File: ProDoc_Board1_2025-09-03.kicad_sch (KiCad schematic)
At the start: 14 parts, among them CN10 A2502-WV02, CN11 A2502-WV02, CN2 B04B-XNISK-A-1(LF)(SN), CN3 B04B-XNISK-A-1(LF)(SN), CN4 B04B-XNISK-A-1(LF)(SN), CN7 XH2.54-5PIN, CN8 A2502-WV02, CN9 A2502-WV02, J1 Conn_01x05_Pin, U3 Ra-02, U4 XL 4005

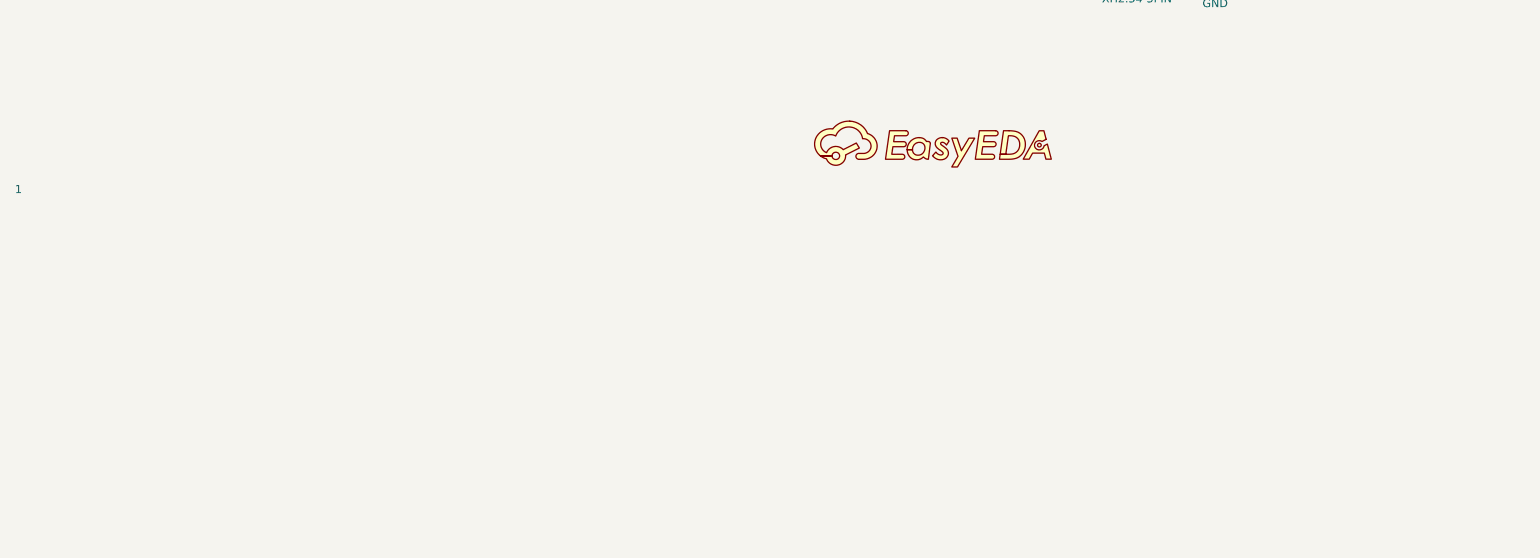
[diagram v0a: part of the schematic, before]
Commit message: added IC
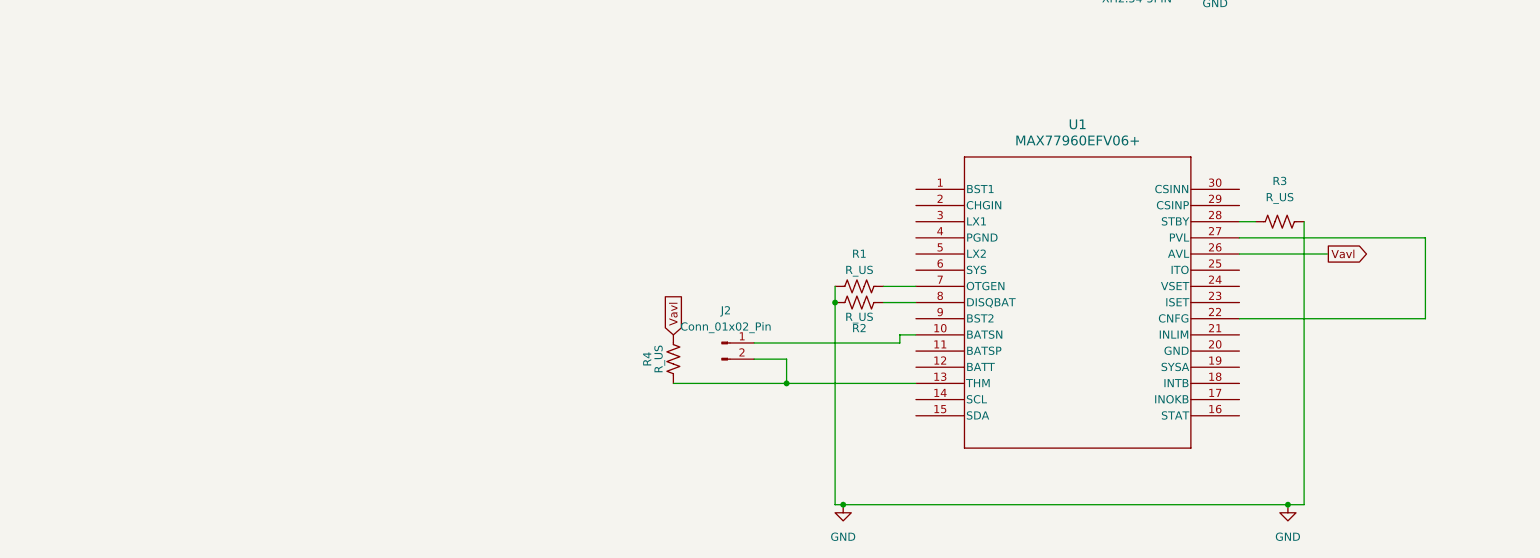
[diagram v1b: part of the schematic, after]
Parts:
- removed 1: ~, symbol ProDoc_Boa-easyedapro:Drawing-Symbol_A4
- added J2: Conn_01x02_Pin, symbol Connector:Conn_01x02_Pin
- added R1, R2, R3, R4: R_US, symbol Device:R_US
- added U1: MAX77960EFV06+, ProDoc_Board1_2025-09-03:MAXIM, symbol MAXIM:MAX77960EFV06+
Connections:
- net GND: now also R1.1, R2.1, R3.2
- new net: R1.2, U1.7 (OTGEN)
- new net: J2.1 (Pin_1), U1.10 (BATSN)
- new net: J2.2 (Pin_2), R4.2, U1.13 (THM)
- new net: U1.22 (CNFG), U1.27 (PVL)
- new net: R3.1, U1.28 (STBY)
- new net: R2.2, U1.8 (DISQBAT)
- new net Vavl: R4.1, U1.26 (AVL)

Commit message: schenatic done
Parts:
- removed U1: MAX77960EFV06+, ProDoc_Board1_2025-09-03:MAXIM, symbol MAXIM:MAX77960EFV06+
- added C1: C_STAT, Capacitor_SMD:C_1210_3225Metric, symbol Device:C_Small
- added C10: C_CSINN, Capacitor_SMD:C_1210_3225Metric, symbol Device:C_Small
- added C11: C_CINP, Capacitor_SMD:C_1210_3225Metric, symbol Device:C_Small
- added C12: C_DIFF, Capacitor_SMD:C_1210_3225Metric, symbol Device:C_Small
- added C2: C_PVL, Capacitor_SMD:C_0402_1005Metric, symbol Device:C_Small
- added C3: C_AVL, Capacitor_SMD:C_0402_1005Metric, symbol Device:C_Small
- added C4: C_BST2, Capacitor_SMD:C_0402_1005Metric, symbol Device:C_Small
- added C5: C_BST1, Capacitor_SMD:C_0402_1005Metric, symbol Device:C_Small
- added C6: C_BATT, Capacitor_SMD:C_0805_2012Metric, symbol Device:C_Small
- added C7: C_OUT1, Capacitor_SMD:C_1210_3225Metric_Pad1.33x2.70mm_HandSolder, symbol Device:C_Small
- added C8: C_OUT2, Capacitor_SMD:C_1210_3225Metric_Pad1.33x2.70mm_HandSolder, symbol Device:C_Small
- added C9: C_CHGIN, Capacitor_SMD:C_1210_3225Metric, symbol Device:C_Small
- added D1: LED, Diode_SMD:D_01005_0402Metric, symbol Device:LED
- added D3: D_Schottky_Small, Diode_SMD:D_SOD-323, symbol Device:D_Schottky_Small
- added L1: L, ProDoc_Board1_2025-09-03:CMLE063T-2R2MS, symbol Device:L
- added R10: R_ITO, Resistor_SMD:R_0805_2012Metric, symbol Device:R_US
- added R11: R_VSET, Resistor_SMD:R_0805_2012Metric, symbol Device:R_US
- added R12: R_INTB, Resistor_SMD:R_0805_2012Metric, symbol Device:R_US
- added R13: R_SDA, Resistor_SMD:R_0805_2012Metric, symbol Device:R_US
- added R14: R_SCL, Resistor_SMD:R_0805_2012Metric, symbol Device:R_US
- added R15, R16: R_SENSE, Resistor_SMD:R_1206_3216Metric, symbol Device:R_US
- added R17: R_CINN, Resistor_SMD:R_1206_3216Metric, symbol Device:R_US
- added R5: R_ISET, Resistor_SMD:R_0805_2012Metric, symbol Device:R_US
- added R6: R_INOKB, Resistor_SMD:R_0805_2012Metric, symbol Device:R_US
- added R7: R_STAT, Resistor_SMD:R_0805_2012Metric, symbol Device:R_US
- added R8: R_PVL, Resistor_SMD:R_0805_2012Metric, symbol Device:R_US
- added R9: R_INLIM, Resistor_SMD:R_0805_2012Metric, symbol Device:R_US
- added U1: MAX77961EFV06+, ProDoc_Board1_2025-09-03:MAX77961, symbol MAX77961:MAX77961EFV06+
- CN10: value A2502-WV02 -> BATT
- CN11: value A2502-WV02 -> CHGIN
- J2: footprint (none) -> Connector_JST:JST_SH_BM02B-SRSS-TB_1x02-1MP_P1.00mm_Vertical
- R1: value R_US -> R_OTGEN; footprint (none) -> Resistor_SMD:R_0805_2012Metric
- R2: value R_US -> R_DISQBAT; footprint (none) -> Resistor_SMD:R_0805_2012Metric
- R3: value R_US -> R_STBY; footprint (none) -> Resistor_SMD:R_0805_2012Metric
- R4: value R_US -> R_TB; footprint (none) -> Resistor_SMD:R_0805_2012Metric
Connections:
- net GND: now also CN11.1, J2.1 (Pin_1), C1.2, C10.2, C11.1, C2.2, C3.2, C6.2, C7.2, C8.2, C9.2, R10.2, R11.2, R5.2, R9.2, U1.10 (BATSN), U1.20 (GND), U1.4 (PGND)
- net BATT+: now reaches CN10.2
- net BATT+: now also C6.1, U1.11 (BATSP), U1.12 (BATT); no longer CN11.1
- net at R1.2: now also U1.7 (OTGEN)
- net at J2.2 (Pin_2), R4.2: now also U1.13 (THM)
- net at R3.1: now also U1.28 (STBY)
- net at R2.2: now also U1.8 (DISQBAT)
- net STAT: now reaches H1.36
- net STAT: now also C1.1, D3.2 (A), R7.1
- net at CN11.2: now also R15.1, R16.2; no longer D2.2 (A)
- net Vavl renamed PULLUP
- net PULLUP: now also C3.1, D1.2 (A), R12.2, R13.1, R14.1, R7.2, R8.2, U1.26 (AVL)
- new net: R14.2, U1.14 (SCL)
- new net: D3.1 (K), U1.16 (STAT)
- new net: R11.1, U1.24 (VSET)
- new net: C2.1, R8.1, U1.22 (CNFG), U1.27 (PVL)
- new net: R6.1, U1.17 (INOKB)
- new net: D1.1 (K), R6.2
- new net: C5.1, U1.1 (BST1)
- new net: C5.2, L1.1, U1.3 (LX1)
- new net: R10.1, U1.25 (ITO)
- new net: R9.1, U1.21 (INLIM)
- new net: R13.2, U1.15 (SDA)
- new net: C4.1, L1.2, U1.5 (LX2)
- new net: C4.2, U1.9 (BST2)
- new net: R12.1, U1.18 (INTB)
- new net: R5.1, U1.23 (ISET)
- new net CHGIN: C9.1, R15.2, R17.2, U1.2 (CHGIN)
- new net CSINN: C10.1, C12.2, R17.1, U1.30 (CSINN)
- new net CSINP: C11.2, C12.1, R16.1, U1.29 (CSINP)
- new net SYS: C7.1, C8.1, D2.2 (A), U1.19 (SYSA), U1.6 (SYS)
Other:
- moved on the sheet: CN10, CN11, D2, R4

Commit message: layout started
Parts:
- C10, C11, C12: footprint Capacitor_SMD:C_1210_3225Metric -> Capacitor_SMD:C_0402_1005Metric
- C7, C8: footprint Capacitor_SMD:C_1210_3225Metric_Pad1.33x2.70mm_HandSolder -> Capacitor_SMD:C_1210_3225Metric
- CN10, CN11: footprint Connector_JST:JST_SH_BM02B-SRSS-TB_1x02-1MP_P1.00mm_Vertical -> Connector_JST:JST_VH_B2P-VH_1x02_P3.96mm_Vertical
- R16: value R_SENSE -> R_CSINP; footprint Resistor_SMD:R_1206_3216Metric -> Resistor_SMD:R_0402_1005Metric
- R17: footprint Resistor_SMD:R_1206_3216Metric -> Resistor_SMD:R_0402_1005Metric
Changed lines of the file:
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@@
 			)
 		)
-		(property "Footprint" "Capacitor_SMD:C_1210_3225Metric_Pad1.33x2.70mm_HandSolder"
+		(property "Footprint" "Capacitor_SMD:C_1210_3225Metric"
 			(at 60.96 26.67 0)
 			(effects
@@
 			)
 		)
-		(property "Footprint" "Connector_JST:JST_SH_BM02B-SRSS-TB_1x02-1MP_P1.00mm_Vertical"
+		(property "Footprint" "Connector_JST:JST_VH_B2P-VH_1x02_P3.96mm_Vertical"
 			(at 69.85 40.64 0)
 			(effects
@@
 		(dnp no)
 		(property "Reference" "R17"
-			(at 32.258 28.448 90)
+			(at 29.972 27.94 90)
 			(effects
 				(font
@@
 		)
 		(property "Value" "R_CINN"
-			(at 35.306 28.448 90)
+			(at 32.258 28.448 90)
 			(effects
 				(font
@@
 			)
 		)
-		(property "Footprint" "Resistor_SMD:R_1206_3216Metric"
+		(property "Footprint" "Resistor_SMD:R_0402_1005Metric"
 			(at 33.274 27.686 90)
 			(effects
@@
 		(dnp no)
 		(property "Reference" "C9"
-			(at 38.354 30.4862 0)
+			(at 39.116 30.4862 0)
 			(effects
 				(font
@@
 		)
 		(property "Value" "C_CHGIN"
-			(at 38.354 28.4542 0)
+			(at 39.116 28.4542 0)
 			(effects
 				(font
@@
 		(dnp no)
 		(property "Reference" "C10"
-			(at 40.6462 35.306 0)
+			(at 40.1382 44.704 0)
 			(effects
 				(font
@@
 		)
 		(property "Value" "C_CSINN"
-			(at 38.6142 35.306 0)
+			(at 38.3602 44.704 0)
 			(effects
 				(font
@@
 			)
 		)
-		(property "Footprint" "Capacitor_SMD:C_1210_3225Metric"
+		(property "Footprint" "Capacitor_SMD:C_0402_1005Metric"
 			(at 36.83 35.56 0)
 			(effects
@@
 		(dnp no)
 		(property "Reference" "C11"
-			(at 25.4062 36.576 0)
+			(at 21.5962 42.926 0)
 			(effects
 				(font
@@
 		)
 		(property "Value" "C_CINP"
-			(at 23.3742 36.576 0)
+			(at 19.5642 44.45 0)
 			(effects
 				(font
@@
 			)
 		)
-		(property "Footprint" "Capacitor_SMD:C_1210_3225Metric"
+		(property "Footprint" "Capacitor_SMD:C_0402_1005Metric"
 			(at 21.59 36.83 0)
 			(effects
@@
 		(dnp no)
 		(property "Reference" "C12"
-			(at 33.0262 35.306 0)
+			(at 30.7402 38.608 90)
 			(effects
 				(font
@@
 		)
 		(property "Value" "C_DIFF"
-			(at 30.9942 35.306 0)
+			(at 32.5182 40.386 90)
 			(effects
 				(font
@@
 			)
 		)
-		(property "Footprint" "Capacitor_SMD:C_1210_3225Metric"
+		(property "Footprint" "Capacitor_SMD:C_0402_1005Metric"
 			(at 29.21 35.56 0)
 			(effects
@@
 		)
 		(property "Value" "R_SENSE"
-			(at 33.274 22.606 90)
+			(at 28.956 20.32 90)
 			(effects
 				(font
@@
 					(size 1.27 1.27)
 				)
+				(hide yes)
 			)
 		)
@@
 		)
 		(property "Value" "CHGIN"
-			(at 13.97 30.48 0)
+			(at 19.558 32.258 0)
 			(effects
 				(font
@@
 			)
 		)
-		(property "Footprint" "Connector_JST:JST_SH_BM02B-SRSS-TB_1x02-1MP_P1.00mm_Vertical"
+		(property "Footprint" "Connector_JST:JST_VH_B2P-VH_1x02_P3.96mm_Vertical"
 			(at 16.51 25.4 0)
 			(effects
@@
 		(dnp no)
 		(property "Reference" "R16"
-			(at 22.098 28.448 90)
+			(at 28.194 27.94 90)
 			(effects
 				(font
@@
 			)
 		)
-		(property "Value" "R_SENSE"
-			(at 22.606 23.876 90)
+		(property "Value" "R_CSINP"
+			(at 26.162 29.21 90)
 			(effects
 				(font
@@
 			)
 		)
-		(property "Footprint" "Resistor_SMD:R_1206_3216Metric"
+		(property "Footprint" "Resistor_SMD:R_0402_1005Metric"
 			(at 23.114 27.686 90)
 			(effects
@@
 			)
 		)
-		(property "Footprint" "Capacitor_SMD:C_1210_3225Metric_Pad1.33x2.70mm_HandSolder"
+		(property "Footprint" "Capacitor_SMD:C_1210_3225Metric"
 			(at 57.15 26.67 0)
 			(effects

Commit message: temp
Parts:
- added C13: C_SYSA, Capacitor_SMD:C_1210_3225Metric, symbol Device:C_Small
- added NT1, NT2: NetTie_2, symbol Device:NetTie_2
- CN10, CN11: footprint Connector_JST:JST_VH_B2P-VH_1x02_P3.96mm_Vertical -> Connector_JST:JST_XH_B2B-XH-A_1x02_P2.50mm_Vertical
- R1, R10, R11, R12, R13, R14, R2, R3, R4, R5, R6, R7, R8, R9: footprint Resistor_SMD:R_0805_2012Metric -> Resistor_SMD:R_0402_1005Metric
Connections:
- net GND: now also C13.2, NT1.1, NT1.2, NT2.1; no longer CN10.1, J2.1 (Pin_1), U1.10 (BATSN)
- net SYS: now also C13.1
- new net BATT-: CN10.1, J2.1 (Pin_1), NT2.2, U1.10 (BATSN)

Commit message: layout started
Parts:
- removed NT1: NetTie_2, symbol Device:NetTie_2
- C13: footprint Capacitor_SMD:C_1210_3225Metric -> Capacitor_SMD:C_0402_1005Metric
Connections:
- net LX1: now reaches C5.2, L1.1, U1.3 (LX1)
- net LX2: now reaches C4.1, L1.2, U1.5 (LX2)
- net VBUS: now reaches CN11.2, R15.1, R16.2
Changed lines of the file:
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@@
 	)
 	(junction
+		(at 21.59 24.13)
+		(diameter 0)
+		(color 0 0 0 0)
+	)
+	(junction
 		(at 59.69 180.34)
 		(diameter 0)
@@
 	(wire
 		(pts
-			(xy 57.15 152.4) (xy 60.96 152.4)
-		)
-		(stroke
-			(width 0)
-			(type default)
-		)
-	)
-	(wire
-		(pts
 			(xy 60.96 24.13) (xy 63.5 24.13)
 		)
@@
 	(wire
 		(pts
+			(xy 52.07 152.4) (xy 60.96 152.4)
+		)
+		(stroke
+			(width 0)
+			(type default)
+		)
+	)
+	(wire
+		(pts
 			(xy 127 60.96) (xy 127 62.23)
 		)
@@
 	(wire
 		(pts
+			(xy 21.59 17.78) (xy 21.59 24.13)
+		)
+		(stroke
+			(width 0)
+			(type default)
+		)
+	)
+	(wire
+		(pts
 			(xy 91.44 64.77) (xy 91.44 74.93)
 		)
@@
 		)
 	)
+	(label "LX1"
+		(at 35.56 162.56 0)
+		(effects
+			(font
+				(size 1.27 1.27)
+			)
+			(justify left bottom)
+		)
+	)
+	(label "LX2"
+		(at 44.45 165.1 0)
+		(effects
+			(font
+				(size 1.27 1.27)
+			)
+			(justify left bottom)
+		)
+	)
+	(label "VBUS"
+		(at 21.59 17.78 0)
+		(effects
+			(font
+				(size 1.27 1.27)
+			)
+			(justify left bottom)
+		)
+	)
 	(global_label "Vavl"
 		(shape input)
@@
 		(dnp no)
 		(property "Reference" "R1"
-			(at 42.672 171.45 90)
+			(at 19.304 171.704 90)
 			(effects
 				(font
@@
 		)
 		(property "Value" "R_OTGEN"
-			(at 48.514 171.704 90)
+			(at 25.4 171.704 90)
 			(effects
 				(font
@@
 			)
 		)
-		(property "Footprint" "Capacitor_SMD:C_1210_3225Metric"
+		(property "Footprint" "Capacitor_SMD:C_0402_1005Metric"
 			(at 53.34 35.56 0)
 			(effects
@@
 		(dnp no)
 		(property "Reference" "R2"
-			(at 42.164 174.244 90)
+			(at 19.304 174.244 90)
 			(effects
 				(font
@@
 		)
 		(property "Value" "R_DISQBAT"
-			(at 48.768 174.244 90)
+			(at 25.908 174.244 90)
 			(effects
 				(font
@@
 	)
 	(symbol
-		(lib_id "Device:NetTie_2")
-		(at 54.61 152.4 0)
-		(unit 1)
-		(exclude_from_sim no)
-		(in_bom no)
-		(on_board yes)
-		(dnp no)
-		(fields_autoplaced yes)
-		(property "Reference" "NT1"
-			(at 54.61 147.32 0)
-			(effects
-				(font
-					(size 1.27 1.27)
-				)
-			)
-		)
-		(property "Value" "NetTie_2"
-			(at 54.61 149.86 0)
-			(effects
-				(font
-					(size 1.27 1.27)
-				)
-			)
-		)
-		(property "Footprint" ""
-			(at 54.61 152.4 0)
-			(effects
-				(font
-					(size 1.27 1.27)
-				)
-				(hide yes)
-			)
-		)
-		(property "Datasheet" "~"
-			(at 54.61 152.4 0)
-			(effects
-				(font
-					(size 1.27 1.27)
-				)
-				(hide yes)
-			)
-		)
-		(property "Description" "Net tie, 2 pins"
-			(at 54.61 152.4 0)
-			(effects
-				(font
-					(size 1.27 1.27)
-				)
-				(hide yes)
-			)
-		)
-		(pin "1"
-		)
-		(pin "2"
-		)
-		(instances
-			(project ""
-				(path "/22951858-26de-4467-a87e-6fd549154140"
-					(reference "NT1")
-					(unit 1)
-				)
-			)
-		)
-	)
-	(symbol
 		(lib_id "power:GND")
 		(at 53.34 38.1 0)
@@
 		)
 		(property "Value" "R_STBY"
-			(at 124.968 161.29 90)
+			(at 124.968 161.544 90)
 			(effects
 				(font

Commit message: v1.2.0
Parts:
- removed D1: LED, Diode_SMD:D_01005_0402Metric, symbol Device:LED
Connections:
- net PULLUP: now also R6.2
- net SCL: now reaches R14.2, U1.14 (SCL)
- net SCL: now also CN2.2, CN3.2, CN4.2, H1.5
- net SDA: now reaches CN2.3, CN3.3, CN4.3, H1.3
- net SDA: now also R13.2, U1.15 (SDA)
- net INOKB: now reaches R6.1, U1.17 (INOKB)
- net INOKB: now also H1.38
- net INTB: now reaches H1.40
- net INTB: now also R12.1, U1.18 (INTB)
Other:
- moved on the sheet: R12, R13, R14, R6

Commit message: fixed grounds
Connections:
- net BATT- is gone; now on net GND: CN10.1, J2.1 (Pin_1), NT2.2, U1.10 (BATSN)
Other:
- moved on the sheet: C13, C7, C8, CN10, D2, U4
